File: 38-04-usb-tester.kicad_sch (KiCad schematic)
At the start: 33 parts, among them J1 USB3_A, J2 USB_B_Micro, J3 USB_C_Receptacle, J4 USB_B_Mini

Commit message: changed to usb port 24 pins
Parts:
- removed J3: USB_C_Receptacle, Connector_USB:USB_C_Receptacle_GCT_USB4085, symbol Connector:USB_C_Receptacle
- added J3, J6: 10137061-00021LF, EXT_usb-c-10137061_00021LF:AMPHENOL_10137061-00021LF, symbol SM_usb-c-10137061_00021LF:10137061-00021LF
- J2: value USB_B_Micro -> B_USB_B_Micro
- J4: value USB_B_Mini -> B_USB_B_Mini
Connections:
- net Vcc: no longer J1.1 (VBUS), J1.10 (SHIELD), J1.2 (D-), J1.3 (D+), J1.4 (GND), J1.5 (SSRX-), J1.6 (SSRX+), J1.7 (DRAIN), J1.8 (SSTX-), J1.9 (SSTX+)
- new net A_CC1: J3.A5 (CC1)
- new net A_CC2: J3.B5 (CC2)
- new net A_D1+: J3.A6 (DP1)
- new net A_D1-: J3.A7 (DN1)
- new net A_D2+: J3.B6 (DP2)
- new net A_D2-: J3.B7 (DN2)
- new net A_GND_1: J3.A1 (GND_A1)
- new net A_GND_2: J3.A12 (GND_A12)
- new net A_GND_3: J3.B1 (GND_B1)
- new net A_GND_4: J3.B12 (GND_B12)
- new net A_SBU1: J3.A8 (SBU1)
- new net A_SBU2: J3.B8 (SBU2)
- new net A_SHIELD: J3.S1 (SHIELD), J3.S2 (SHIELD__1), J3.S3 (SHIELD__2), J3.S4 (SHIELD__3)
- new net A_SSRTx1+: J3.A2 (SSTXP1)
- new net A_SSRx1+: J3.B11 (SSRXP1)
- new net A_SSRx1-: J3.A3 (SSTXN1), J3.B10 (SSRXN1)
- new net A_SSRx2+: J3.A11 (SSRXP2)
- new net A_SSRx2-: J3.A10 (SSRXN2)
- new net A_SSTx2+: J3.B2 (SSTXP2)
- new net A_SSTx2-: J3.B3 (SSTXN2)
- new net A_VBUS_A4: J3.A4 (VBUS_A4)
- new net A_VBUS_A9: J3.A9 (VBUS_A9)
- new net A_VBUS_B4: J3.B4 (VBUS_B4)
- new net A_VBUS_B9: J3.B9 (VBUS_B9)
- no-connect marks 6 -> 0
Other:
- note added: "B Side - Provides Power"
- note removed: "B Side"
- moved on the sheet: D_CC1, D_CC2, D_Dn1, D_Dn2, D_Dp1, D_Dp2, D_GND1, D_SHLD1, D_SSRxn1, D_SSRxp1, D_SSTxn1, D_SSTxp1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

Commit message: direct led connections
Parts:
- removed D_CC1, D_CC2, D_Dn1, D_Dn2, D_Dp1, D_Dp2, D_GND1, D_SHLD1, D_SSRxn1, D_SSRxp1, D_SSTxn1, D_SSTxp1, D_VBUS1: LED, LED_SMD:LED_0805_2012Metric, symbol Device:LED
- removed JP1: SolderJumper_2_Open, Jumper:SolderJumper-2_P1.3mm_Open_RoundedPad1.0x1.5mm, symbol Jumper:SolderJumper_2_Open
- removed R1, R10, R11, R12, R13, R2, R3, R4, R5, R6, R7, R8, R9: 100, Resistor_SMD:R_0805_2012Metric, symbol Device:R
- added D, D12, D8: SSRx2-_D, LED_SMD:LED_0805_2012Metric, symbol Device:LED
- added D1, D13, D9: SSRx2+_D, LED_SMD:LED_0805_2012Metric, symbol Device:LED
- added D10, D2: SSRx1+_D, LED_SMD:LED_0805_2012Metric, symbol Device:LED
- added D11, D3: SSRx1-_D, LED_SMD:LED_0805_2012Metric, symbol Device:LED
- added D4: SSTx2-_D, LED_SMD:LED_0805_2012Metric, symbol Device:LED
- added D5: SSTx2+_D, LED_SMD:LED_0805_2012Metric, symbol Device:LED
- added D6: SSTx1+_D, LED_SMD:LED_0805_2012Metric, symbol Device:LED
- added D7: SSTx1-_D, LED_SMD:LED_0805_2012Metric, symbol Device:LED
- added RN1, RN2, RN3, RN4, RN5, RN6: R_Pack03, symbol Device:R_Pack03
- added U1: RP2040, Package_DFN_QFN:QFN-56-1EP_7x7mm_P0.4mm_EP3.2x3.2mm, symbol MCU_RaspberryPi:RP2040
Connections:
- net A_GND_1 is gone; now on net GND: J3.A1 (GND_A1)
- net A_GND_2 is gone; now on net GND: J3.A12 (GND_A12)
- net A_GND_3 is gone; now on net GND: J3.B1 (GND_B1)
- net A_GND_4 is gone; now on net GND: J3.B12 (GND_B12)
- net Dn1 is gone; now on net B_D1-: J2.2 (D-), J4.2 (D-)
- net Dp1 is gone; now on net B_D1+: J2.3 (D+), J4.3 (D+)
- net GROUND is gone; now on net GND: J2.5 (GND), J4.5 (GND)
- net A_CC1: now also J6.A5 (CC1); no longer J3.A5 (CC1)
- net A_CC2: now also J6.B5 (CC2); no longer J3.B5 (CC2)
- net A_VBUS_A4: now also J1.1 (VBUS), J6.A4 (VBUS_A4); no longer J3.A4 (VBUS_A4)
- net A_VBUS_A9: now also J6.A9 (VBUS_A9); no longer J3.A9 (VBUS_A9)
- net A_VBUS_B4: now also J6.B4 (VBUS_B4); no longer J3.B4 (VBUS_B4)
- net A_VBUS_B9: now also J6.B9 (VBUS_B9); no longer J3.B9 (VBUS_B9)
- net GND: now also D.1 (K), D1.1 (K), D10.1 (K), D11.1 (K), D12.1 (K), D13.1 (K), D2.1 (K), D3.1 (K), D4.1 (K), D5.1 (K), D6.1 (K), D7.1 (K), D9.1 (K)
- net ID: now reaches J2.4 (ID)
- net ID: now also J4.4 (ID)
- net A_D1-_D: now reaches J1.2 (D-)
- net A_D1-_D: now also J6.A7 (DN1), D9.2 (A)
- net A_D1+_D: now reaches J1.3 (D+)
- net A_D1+_D: now also J6.A6 (DP1), D8.2 (A)
- net A_SSRx1-_D: now reaches J1.5 (SSRX-)
- net A_SSRx1-_D: now also J6.B10 (SSRXN1), D3.2 (A)
- net A_SSRx1+_D: now reaches J1.6 (SSRX+)
- net A_SSRx1+_D: now also J6.B11 (SSRXP1), D2.2 (A)
- net A_SSTx1-_D: now reaches J1.8 (SSTX-)
- net A_SSTx1-_D: now also J6.A3 (SSTXN1), D7.2 (A)
- net A_SSTx1+_D: now reaches J1.9 (SSTX+)
- net A_SSTx1+_D: now also J6.A2 (SSTXP1), D6.2 (A)
- net A_GND: now reaches J6.A1 (GND_A1)
- net A_GND: now also J6.A12 (GND_A12), J6.B1 (GND_B1), J6.B12 (GND_B12)
- net A_SSRx2-_D: now reaches J6.A10 (SSRXN2)
- net A_SSRx2-_D: now also D.2 (A)
- net A_SSRx2+_D: now reaches J6.A11 (SSRXP2)
- net A_SSRx2+_D: now also D1.2 (A)
- net A_SBU1_D: now reaches J6.A8 (SBU1)
- net A_SBU1_D: now also D12.2 (A)
- net A_SSTx2+_D: now reaches J6.B2 (SSTXP2)
- net A_SSTx2+_D: now also D5.2 (A)
- net A_SSTx2-_D: now reaches J6.B3 (SSTXN2)
- net A_SSTx2-_D: now also D4.2 (A)
- net A_D2+_D: now reaches J6.B6 (DP2)
- net A_D2+_D: now also D11.2 (A)
- net A_D2-_D: now reaches J6.B7 (DN2)
- net A_D2-_D: now also D10.2 (A)
- net A_SBU2_D: now reaches J6.B8 (SBU2)
- net A_SBU2_D: now also D13.2 (A)
- net A_D1+ renamed B_D1+
- net B_D1+: now also RN5.3 (R3.1)
- net A_D1- renamed B_D1-
- net B_D1-: now also RN5.2 (R2.1)
- net A_D2+ renamed B_D2+
- net B_D2+: now also RN2.6 (R1.2)
- net A_D2- renamed B_D2-
- net B_D2-: now also RN2.5 (R2.2)
- net A_SBU1 renamed B_SBU1
- net B_SBU1: now also RN5.1 (R1.1)
- net A_SBU2 renamed B_SBU2
- net B_SBU2: now also RN2.4 (R3.2)
- removed net A_SHIELD: J3.S1 (SHIELD), J3.S2 (SHIELD__1), J3.S3 (SHIELD__2), J3.S4 (SHIELD__3)
- net A_SSRTx1+ renamed B_SSRTx1+
- net B_SSRTx1+: now also RN4.3 (R3.1)
- net A_SSRx1+ renamed B_SSRx1+
- net B_SSRx1+: now also RN1.4 (R3.2)
- net A_SSRx1- renamed B_SSRx1-
- net B_SSRx1-: now also RN1.5 (R2.2), RN4.2 (R2.1)
- net A_SSRx2+ renamed B_SSRx2+
- net B_SSRx2+: now also RN6.1 (R1.1)
- net A_SSRx2- renamed B_SSRx2-
- net B_SSRx2-: now also RN6.2 (R2.1)
- net A_SSTx2+ renamed B_SSTx2+
- net B_SSTx2+: now also RN3.6 (R1.2)
- net A_SSTx2- renamed B_SSTx2-
- net B_SSTx2-: now also RN3.5 (R2.2)
- net SHIELD: no longer names the net of J2.6 (Shield)
- net SHIELD: no longer J4.6 (Shield)
- net VBUS renamed B_VBUS_A4
- net B_VBUS_A4: now also J3.A4 (VBUS_A4), RN4.1 (R1.1)
- net Vcc renamed VCC
- net VCC: now also RN1.1 (R1.1), RN1.2 (R2.1), RN1.3 (R3.1), RN2.1 (R1.1), RN2.2 (R2.1), RN2.3 (R3.1), RN3.1 (R1.1), RN3.2 (R2.1), RN3.3 (R3.1), RN4.4 (R3.2), RN4.5 (R2.2), RN4.6 (R1.2), RN5.4 (R3.2), RN5.5 (R2.2), RN5.6 (R1.2), RN6.4 (R3.2), RN6.5 (R2.2), RN6.6 (R1.2)
- new net: U1.1 (IOVDD), U1.10 (IOVDD), U1.22 (IOVDD), U1.33 (IOVDD), U1.42 (IOVDD), U1.49 (IOVDD)
- new net: U1.23 (DVDD), U1.50 (DVDD)
- new net B_CC1: J3.A5 (CC1)
- new net B_CC2: J3.B5 (CC2)
- new net B_VBUS_A9: J3.A9 (VBUS_A9), RN6.3 (R3.1)
- new net B_VBUS_B4: J3.B4 (VBUS_B4), RN3.4 (R3.2)
- new net B_VBUS_B9: J3.B9 (VBUS_B9), RN1.6 (R1.2)
- no-connect marks 0 -> 11
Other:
- note added: "B Side (Provides Power)"
- note added: "TODO - MCU"
- note added: "Wire Connection Direct Check"
- note added: "to mcu to test"
- note removed: "B Side - Provides Power"
- note removed: "TODO"
- moved on the sheet: J1, J2, J3, J4, J6

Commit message: STM32 layout
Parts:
- removed U1: RP2040, Package_DFN_QFN:QFN-56-1EP_7x7mm_P0.4mm_EP3.2x3.2mm, symbol MCU_RaspberryPi:RP2040
- added C2: C, symbol Device:C
- added C3: 100n, symbol Device:C
- added D14, D15, D16, D17, D18, D19, D20, D21: ~, LED_SMD:LED_0805_2012Metric, symbol Device:LED
- added D22: Power, symbol Device:LED
- added J5: Conn_01x05_Pin, symbol Connector:Conn_01x05_Pin
- added R1, R2: R, symbol Device:R
- added R3: 10k, symbol Device:R
- added RN7, RN8: R_Pack04, symbol Device:R_Pack04
- added SW1: SW_SPDT, symbol Switch:SW_SPDT
- added U1: STM32C031K6Tx, Package_QFP:LQFP-32_7x7mm_P0.8mm, symbol MCU_ST_STM32C0:STM32C031K6Tx
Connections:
- net A_VBUS_A9 is gone; now on net A_VBUS_A4: J6.A9 (VBUS_A9)
- net A_VBUS_B4 is gone; now on net A_VBUS_A4: J6.B4 (VBUS_B4)
- net A_VBUS_B9 is gone; now on net A_VBUS_A4: J6.B9 (VBUS_B9)
- net A_CC1: now also U1.13 (PA6)
- net A_CC2: now also U1.14 (PA7)
- net A_VBUS_A4: now also U1.8 (PA1)
- net GND: now also C2.1, C3.2, D14.1 (K), D15.1 (K), D16.1 (K), D17.1 (K), D18.1 (K), D19.1 (K), D20.1 (K), D22.1 (K), J5.1 (Pin_1), U1.5 (VSS)
- net ID: now also D21.1 (K)
- net VCC: now also C2.2, J5.5 (Pin_5), R3.1, RN8.8 (R1.2), SW1.2 (B), U1.4 (VDD); no longer BT1.1 (+), C1.1
- net A_GND renamed A_GND_A1
- net A_GND_A1: now also U1.7 (PA0)
- net B_CC1 renamed B_CC1_SENS
- net B_CC1_SENS: now also R2.2, U1.11 (PA4)
- net B_CC2 renamed B_CC2_SENS
- net B_CC2_SENS: now also R1.2, U1.12 (PA5)
- new net: D15.2 (A), RN7.3 (R3.1)
- new net: D16.2 (A), RN7.2 (R2.1)
- new net: BT1.1 (+), C1.1, SW1.3 (C)
- new net: D19.2 (A), RN8.3 (R3.1)
- new net: D22.2 (A), R3.2
- new net: D20.2 (A), RN8.2 (R2.1)
- new net: D17.2 (A), RN7.1 (R1.1)
- new net: D14.2 (A), RN7.4 (R4.1)
- new net: D18.2 (A), RN8.4 (R4.1)
- new net: D21.2 (A), RN8.1 (R1.1)
- new net CC1_CTRL: R2.1, U1.9 (PA2)
- new net CC2_CTRL: R1.1, U1.10 (PA3)
- new net CC_NORM_LED: RN7.7 (R2.2), U1.17 (PB2)
- new net CC_REV_LED: RN7.8 (R1.2), U1.27 (PB3)
- new net CC_Rd_LED: RN8.6 (R3.2), U1.29 (PB5)
- new net CC_Rp_LED: RN8.5 (R4.2), U1.28 (PB4)
- new net E_MARKER_LED: RN8.7 (R2.2), U1.30 (PB6)
- new net GND_LED: RN7.5 (R4.2), U1.15 (PB0)
- new net SWCLK_BOOT0: J5.3 (Pin_3), U1.25 (PA14)
- new net SWDIO: J5.4 (Pin_4), U1.24 (PA13)
- new net VBUS_LED: RN7.6 (R3.2), U1.16 (PB1)
- new net ~{RESET}: C3.1, J5.2 (Pin_2), U1.6 (PF2)
- no-connect marks 11 -> 12
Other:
- note added: "100nF per STM32C0 ref schematic"
- note added: "Debug & Program"
- note added: "MCU Controlled LEDs"
- note added: "NRESET has internal pullup"
- note added: "Question on Vbus resistor"
- note removed: "Break these out to a separate portion of the board for easy ID of orientation"
- note removed: "TODO - MCU"
- note removed: "Use separate leds for Dp1 and Dp2 since they might not be connected together internally (cheap cable?)"
- note removed: "to mcu to test"
- moved on the sheet: BT1, C1, D, D1, D10, D11, D12, D13, D2, D3, D4, D5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

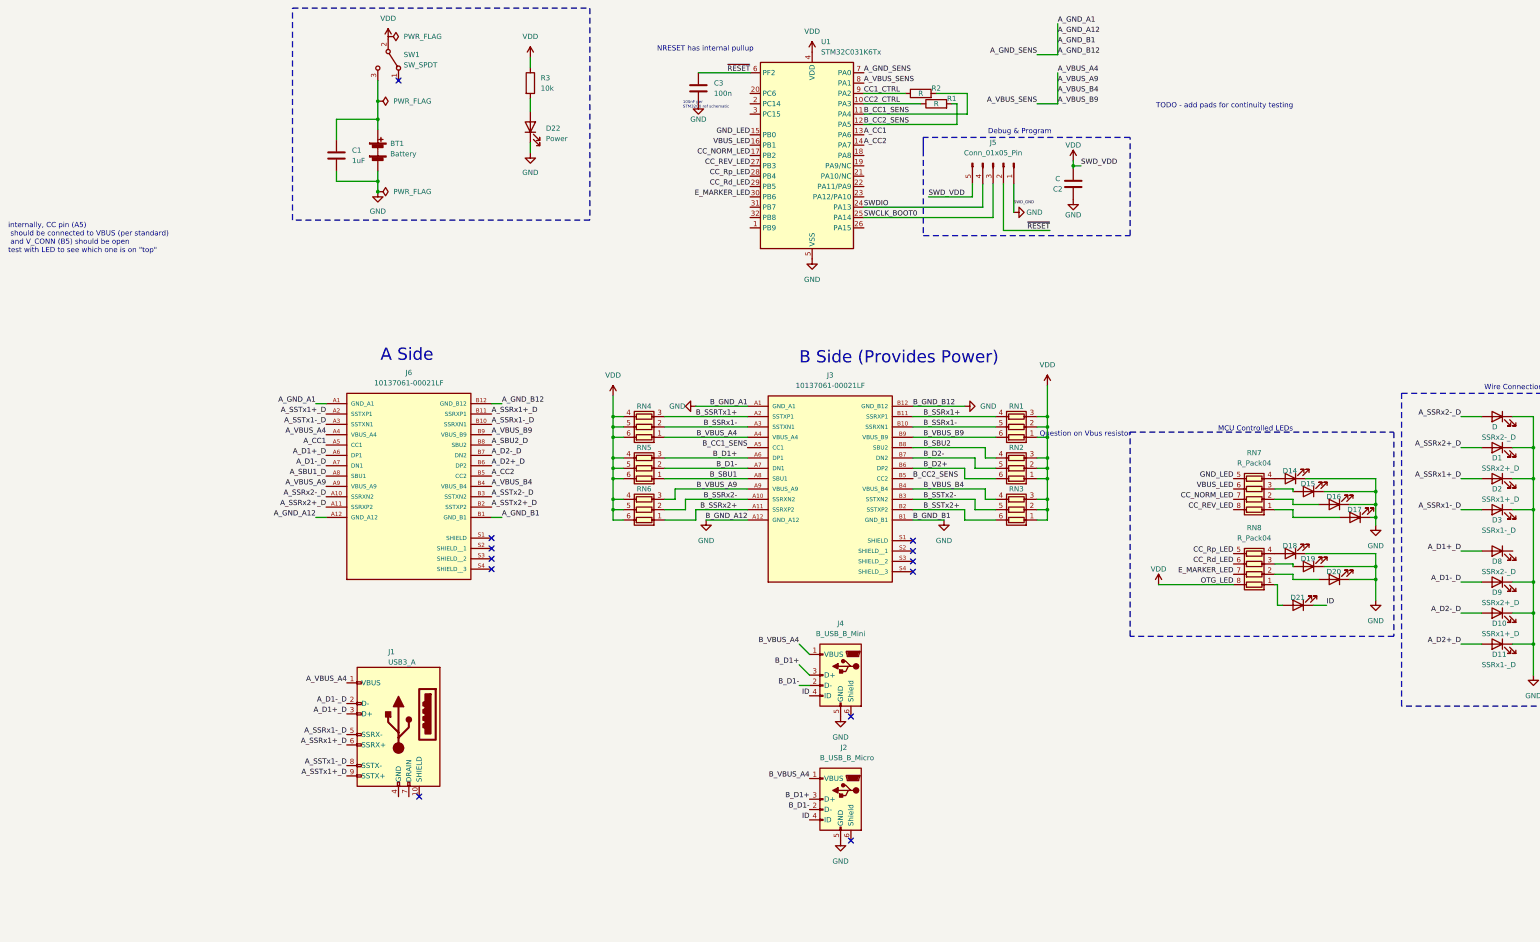
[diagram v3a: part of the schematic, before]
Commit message: added through holes for testing and vbus-sense resistor
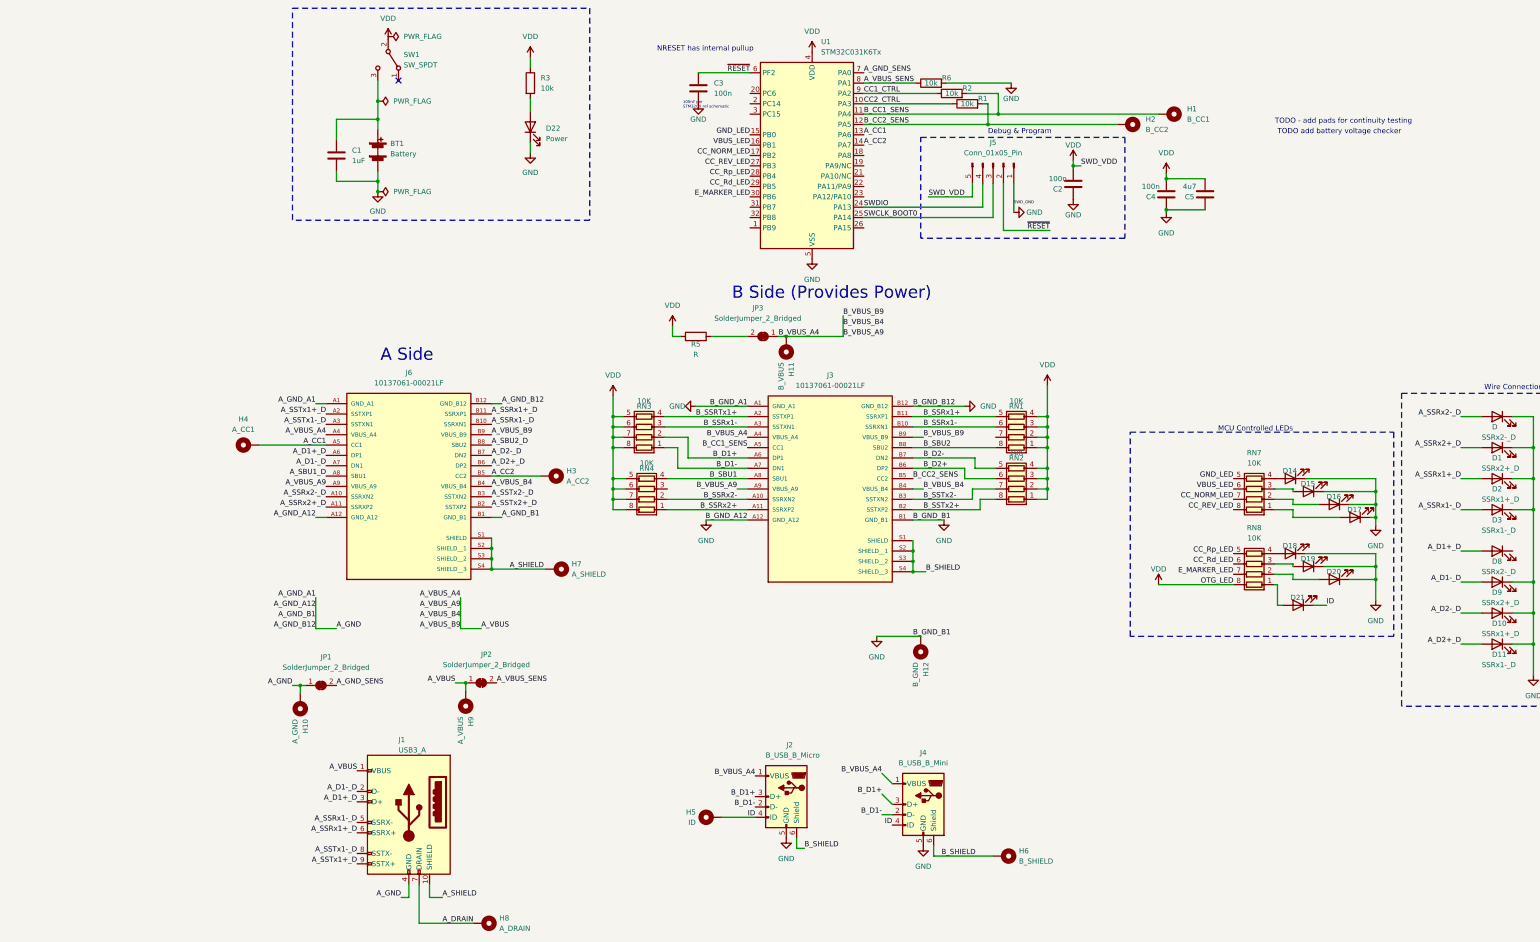
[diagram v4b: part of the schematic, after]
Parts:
- removed RN1, RN2, RN3, RN4, RN5, RN6: R_Pack03, symbol Device:R_Pack03
- added C4: 100n, symbol Device:C
- added C5: 4u7, symbol Device:C
- added H1: B_CC1, symbol Mechanical:MountingHole_Pad
- added H10: A_GND, symbol Mechanical:MountingHole_Pad
- added H11: B_VBUS, symbol Mechanical:MountingHole_Pad
- added H12: B_GND, symbol Mechanical:MountingHole_Pad
- added H2: B_CC2, symbol Mechanical:MountingHole_Pad
- added H3: A_CC2, symbol Mechanical:MountingHole_Pad
- added H4: A_CC1, symbol Mechanical:MountingHole_Pad
- added H5: ID, symbol Mechanical:MountingHole_Pad
- added H6: B_SHIELD, symbol Mechanical:MountingHole_Pad
- added H7: A_SHIELD, symbol Mechanical:MountingHole_Pad
- added H8: A_DRAIN, symbol Mechanical:MountingHole_Pad
- added H9: A_VBUS, symbol Mechanical:MountingHole_Pad
- added JP1, JP2, JP3: SolderJumper_2_Bridged, symbol Jumper:SolderJumper_2_Bridged
- added R5: R, symbol Device:R
- added R6: 10k, symbol Device:R
- added RN1, RN2, RN3, RN4: 10K, symbol Device:R_Pack04
- C2: value C -> 100n
- R1, R2: value R -> 10k
- RN7, RN8: value R_Pack04 -> 10K
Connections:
- net B_VBUS_A9 is gone; now on net B_VBUS_A4: J3.A9 (VBUS_A9)
- net B_VBUS_B4 is gone; now on net B_VBUS_A4: J3.B4 (VBUS_B4)
- net B_VBUS_B9 is gone; now on net B_VBUS_A4: J3.B9 (VBUS_B9)
- net A_CC1: now also H4.1
- net A_CC2: now also H3.1
- net B_CC1_SENS: now also H1.1
- net B_CC2_SENS: now also H2.1
- net B_D1+: now also RN3.2 (R2.1)
- net B_D1-: now also RN3.1 (R1.1)
- net B_D2+: now also RN2.6 (R3.2)
- net B_D2-: now also RN2.5 (R4.2)
- net B_SBU1: now also RN4.4 (R4.1)
- net B_SBU2: now also RN1.8 (R1.2)
- net B_SSRTx1+: now also RN3.4 (R4.1)
- net B_SSRx1+: now also RN1.5 (R4.2)
- net B_SSRx1-: now also RN1.6 (R3.2), RN3.3 (R3.1)
- net B_SSRx2+: now also RN4.1 (R1.1)
- net B_SSRx2-: now also RN4.2 (R2.1)
- net B_SSTx2+: now also RN2.8 (R1.2)
- net B_SSTx2-: now also RN2.7 (R2.2)
- net B_VBUS_A4: now also H11.1, JP3.1 (A)
- net GND: now also C4.1, C5.1, H12.1, R6.2
- net ID: now also H5.1
- net VCC: now also C4.2, C5.2, R5.1, RN1.1 (R1.1), RN1.2 (R2.1), RN1.3 (R3.1), RN1.4 (R4.1), RN2.1 (R1.1), RN2.2 (R2.1), RN2.3 (R3.1), RN2.4 (R4.1), RN3.5 (R4.2), RN3.6 (R3.2), RN3.7 (R2.2), RN3.8 (R1.2), RN4.5 (R4.2), RN4.6 (R3.2), RN4.7 (R2.2), RN4.8 (R1.2)
- net B_SHIELD: now reaches J2.6 (Shield)
- net B_SHIELD: now also J3.S1 (SHIELD), J3.S2 (SHIELD__1), J3.S3 (SHIELD__2), J3.S4 (SHIELD__3), J4.6 (Shield), H6.1
- net A_SHIELD: now reaches J1.10 (SHIELD)
- net A_SHIELD: now also J6.S1 (SHIELD), J6.S2 (SHIELD__1), J6.S3 (SHIELD__2), J6.S4 (SHIELD__3), H7.1
- net A_GND: now reaches J1.4 (GND)
- net A_GND: now also J6.A1 (GND_A1), J6.A12 (GND_A12), J6.B1 (GND_B1), J6.B12 (GND_B12), H10.1, JP1.1 (A)
- net A_DRAIN: now reaches J1.7 (DRAIN)
- net A_DRAIN: now also H8.1
- removed net A_GND_A1: J6.A1 (GND_A1), J6.A12 (GND_A12), J6.B1 (GND_B1), J6.B12 (GND_B12), U1.7 (PA0)
- net A_VBUS_A4 renamed A_VBUS
- net A_VBUS: now also H9.1, JP2.1 (A); no longer U1.8 (PA1)
- new net: JP3.2 (B), R5.2
- new net A_GND_SENS: JP1.2 (B), U1.7 (PA0)
- new net A_VBUS_SENS: JP2.2 (B), R6.1, U1.8 (PA1)
- no-connect marks 12 -> 1
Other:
- note added: "TODO add battery voltage checker"
- note removed: "Question on Vbus resistor"
- note removed: "internally, CC pin (A5) should be connected to VBUS (per standard) and V_CONN (B5) should be open test with LED to see which one is on "top""
- moved on the sheet: J1, J2, J4, R1, R2
